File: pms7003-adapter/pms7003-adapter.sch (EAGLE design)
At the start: 8 parts, among them J1 LPPB052CFFN-RC, U1 WEMOS-D1-MINI, U2 ATECC508A-SSHDA-T

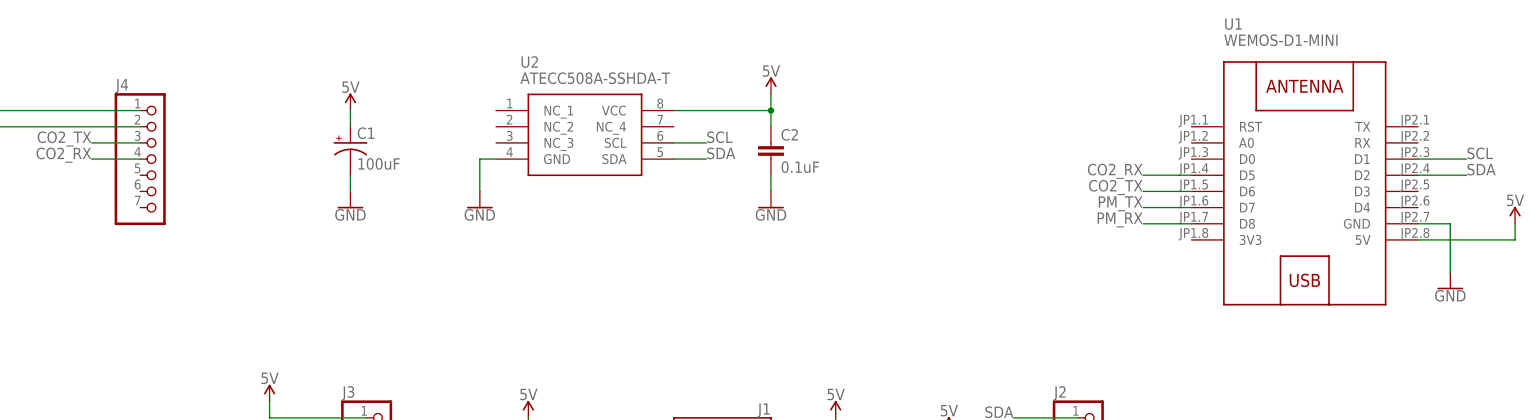
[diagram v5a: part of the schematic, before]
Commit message: Resized CO2 sensor connector, ripped up all traces for redesign
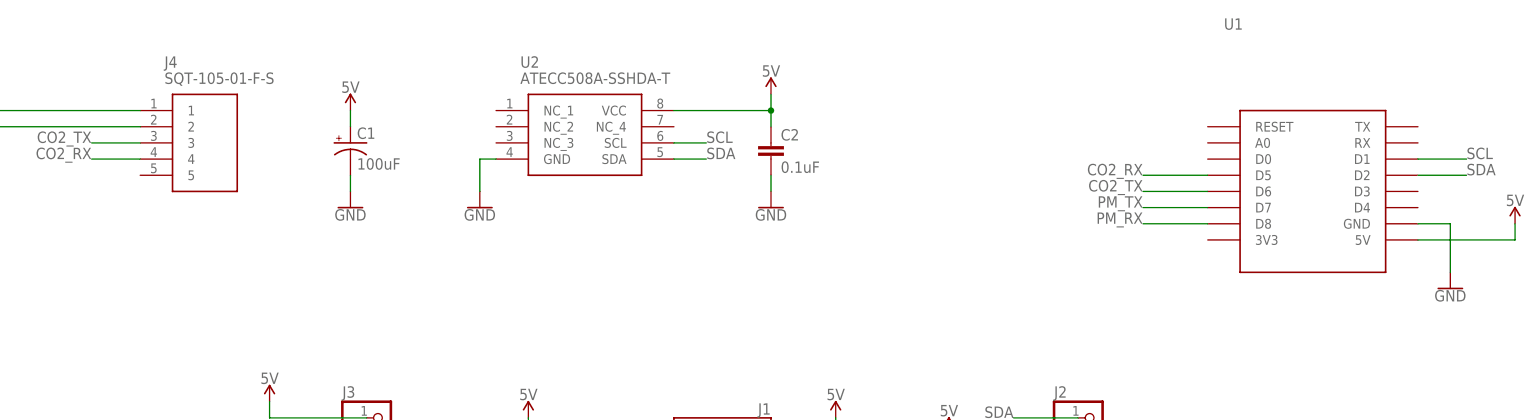
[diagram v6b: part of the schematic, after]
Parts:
- J4: value (none) -> SQT-105-01-F-S; device pinhead:PINHD-1X7 -> aqm-parts:SQT-105-01-F-S
- U1: value WEMOS-D1-MINI -> (none)
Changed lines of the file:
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@@
 <?xml version="1.0" encoding="utf-8"?>
 <!DOCTYPE eagle SYSTEM "eagle.dtd">
-<eagle version="9.6.1">
+<eagle version="9.6.2">
 <drawing>
 <settings>
@@
 <part name="SUPPLY2" library="SparkFun-PowerSymbols" library_urn="urn:adsk.eagle:library:530" deviceset="5V" device=""/>
 <part name="GND1" library="SparkFun-PowerSymbols" deviceset="GND" device=""/>
-<part name="J4" library="pinhead" library_urn="urn:adsk.eagle:library:325" deviceset="PINHD-1X7" device="" package3d_urn="urn:adsk.eagle:package:22477/2"/>
 <part name="SUPPLY1" library="SparkFun-PowerSymbols" library_urn="urn:adsk.eagle:library:530" deviceset="5V" device=""/>
 <part name="GND4" library="SparkFun-PowerSymbols" deviceset="GND" device=""/>
+<part name="J4" library="aqm-parts" deviceset="SQT-105-01-F-S" device=""/>
 </parts>
 <sheets>
@@
 <attribute name="VALUE" x="40.64" y="9.906" size="1.778" layer="96" align="top-center"/>
 </instance>
-<instance part="U1" gate="G$1" x="114.3" y="55.88" smashed="yes">
+<instance part="U1" gate="D1" x="114.3" y="55.88" smashed="yes">
 <attribute name="NAME" x="101.6" y="81.28" size="1.778" layer="95"/>
 <attribute name="VALUE" x="101.6" y="78.74" size="1.778" layer="96"/>
@@
 <attribute name="VALUE" x="137.16" y="40.386" size="1.778" layer="96" align="top-center"/>
 </instance>
-<instance part="J4" gate="A" x="-66.04" y="60.96" smashed="yes">
-<attribute name="NAME" x="-72.39" y="71.755" size="1.778" layer="95"/>
-<attribute name="VALUE" x="-72.39" y="48.26" size="1.778" layer="96"/>
-</instance>
 <instance part="SUPPLY1" gate="G$1" x="-93.98" y="71.12" smashed="yes">
 <attribute name="VALUE" x="-93.98" y="73.914" size="1.778" layer="96" align="bottom-center"/>
@@
 <instance part="GND4" gate="1" x="-93.98" y="60.96" smashed="yes">
 <attribute name="VALUE" x="-93.98" y="60.706" size="1.778" layer="96" align="top-center"/>
+</instance>
+<instance part="J4" gate="G$1" x="-68.58" y="68.58" smashed="yes">
+<attribute name="NAME" x="-64.77" y="76.2" size="1.778" layer="95" align="center-left"/>
+<attribute name="VALUE" x="-64.77" y="73.66" size="1.778" layer="96" align="center-left"/>
 </instance>
 </instances>
@@
 </segment>
 <segment>
-<pinref part="U1" gate="G$1" pin="D8"/>
-<wire x1="96.52" y1="50.8" x2="88.9" y2="50.8" width="0.1524" layer="91"/>
+<pinref part="U1" gate="D1" pin="D8"/>
+<wire x1="99.06" y1="50.8" x2="88.9" y2="50.8" width="0.1524" layer="91"/>
 <label x="88.9" y="50.8" size="1.778" layer="95" rot="MR0"/>
 </segment>
@@
 </segment>
 <segment>
-<pinref part="U1" gate="G$1" pin="D7"/>
-<wire x1="96.52" y1="53.34" x2="88.9" y2="53.34" width="0.1524" layer="91"/>
+<pinref part="U1" gate="D1" pin="D7"/>
+<wire x1="99.06" y1="53.34" x2="88.9" y2="53.34" width="0.1524" layer="91"/>
 <label x="88.9" y="53.34" size="1.778" layer="95" rot="MR0"/>
 </segment>
@@
 </segment>
 <segment>
-<pinref part="U1" gate="G$1" pin="GND"/>
+<pinref part="U1" gate="D1" pin="GND"/>
 <wire x1="132.08" y1="50.8" x2="137.16" y2="50.8" width="0.1524" layer="91"/>
 <pinref part="GND1" gate="1" pin="GND"/>
@@
 <pinref part="GND4" gate="1" pin="GND"/>
 <wire x1="-93.98" y1="63.5" x2="-93.98" y2="66.04" width="0.1524" layer="91"/>
-<pinref part="J4" gate="A" pin="2"/>
 <wire x1="-93.98" y1="66.04" x2="-68.58" y2="66.04" width="0.1524" layer="91"/>
+<pinref part="J4" gate="G$1" pin="2"/>
 </segment>
 </net>
@@
 </segment>
 <segment>
-<pinref part="U1" gate="G$1" pin="5V"/>
+<pinref part="U1" gate="D1" pin="5V"/>
 <wire x1="132.08" y1="48.26" x2="147.32" y2="48.26" width="0.1524" layer="91"/>
 <pinref part="SUPPLY2" gate="G$1" pin="5V"/>
@@
 <pinref part="SUPPLY1" gate="G$1" pin="5V"/>
 <wire x1="-93.98" y1="71.12" x2="-93.98" y2="68.58" width="0.1524" layer="91"/>
-<pinref part="J4" gate="A" pin="1"/>
 <wire x1="-68.58" y1="68.58" x2="-93.98" y2="68.58" width="0.1524" layer="91"/>
+<pinref part="J4" gate="G$1" pin="1"/>
 </segment>
 </net>
@@
 </segment>
 <segment>
-<pinref part="U1" gate="G$1" pin="D2"/>
+<pinref part="U1" gate="D1" pin="D2"/>
 <wire x1="132.08" y1="58.42" x2="139.7" y2="58.42" width="0.1524" layer="91"/>
 <label x="139.7" y="58.42" size="1.778" layer="95"/>
@@
 </segment>
 <segment>
-<pinref part="U1" gate="G$1" pin="D1"/>
+<pinref part="U1" gate="D1" pin="D1"/>
 <wire x1="132.08" y1="60.96" x2="139.7" y2="60.96" width="0.1524" layer="91"/>
 <label x="139.7" y="60.96" size="1.778" layer="95"/>
@@
 <net name="CO2_TX" class="0">
 <segment>
-<pinref part="J4" gate="A" pin="3"/>
 <wire x1="-68.58" y1="63.5" x2="-76.2" y2="63.5" width="0.1524" layer="91"/>
 <label x="-76.2" y="63.5" size="1.778" layer="95" rot="MR0"/>
-</segment>
-<segment>
-<pinref part="U1" gate="G$1" pin="D6"/>
-<wire x1="96.52" y1="55.88" x2="88.9" y2="55.88" width="0.1524" layer="91"/>
+<pinref part="J4" gate="G$1" pin="3"/>
+</segment>
+<segment>
+<pinref part="U1" gate="D1" pin="D6"/>
+<wire x1="99.06" y1="55.88" x2="88.9" y2="55.88" width="0.1524" layer="91"/>
 <label x="88.9" y="55.88" size="1.778" layer="95" rot="MR0"/>
 </segment>
@@
 <net name="CO2_RX" class="0">
 <segment>
-<pinref part="J4" gate="A" pin="4"/>
 <wire x1="-68.58" y1="60.96" x2="-76.2" y2="60.96" width="0.1524" layer="91"/>
 <label x="-76.2" y="60.96" size="1.778" layer="95" rot="MR0"/>
-</segment>
-<segment>
-<pinref part="U1" gate="G$1" pin="D5"/>
-<wire x1="96.52" y1="58.42" x2="88.9" y2="58.42" width="0.1524" layer="91"/>
+<pinref part="J4" gate="G$1" pin="4"/>
+</segment>
+<segment>
+<pinref part="U1" gate="D1" pin="D5"/>
+<wire x1="99.06" y1="58.42" x2="88.9" y2="58.42" width="0.1524" layer="91"/>
 <label x="88.9" y="58.42" size="1.778" layer="95" rot="MR0"/>
 </segment>
@@
 </drawing>
 <compatibility>
+<note version="6.3" minversion="6.2.2" severity="warning">
+Since Version 6.2.2 text objects can contain more than one line,
+which will not be processed correctly with this version.
+</note>
 <note version="8.2" severity="warning">
 Since Version 8.2, EAGLE supports online libraries. The ids

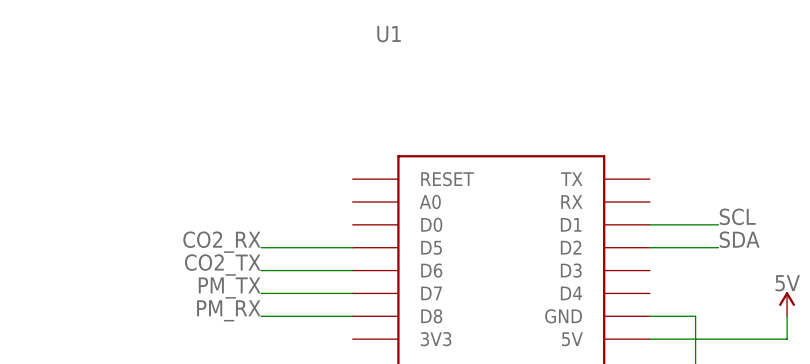
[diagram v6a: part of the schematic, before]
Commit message: Added an improved D1 mini footprint
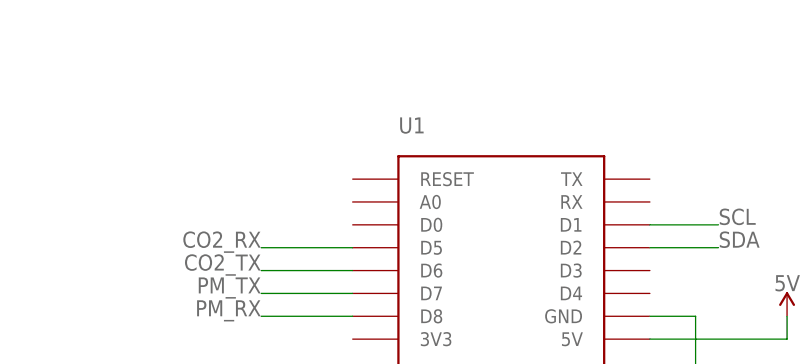
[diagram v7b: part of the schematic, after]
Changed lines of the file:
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@@
 </instance>
 <instance part="U1" gate="D1" x="114.3" y="55.88" smashed="yes">
-<attribute name="NAME" x="101.6" y="81.28" size="1.778" layer="95"/>
+<attribute name="NAME" x="104.14" y="71.12" size="1.778" layer="95"/>
 <attribute name="VALUE" x="101.6" y="78.74" size="1.778" layer="96"/>
 </instance>
@@
 </drawing>
 <compatibility>
-<note version="6.3" minversion="6.2.2" severity="warning">
-Since Version 6.2.2 text objects can contain more than one line,
-which will not be processed correctly with this version.
-</note>
 <note version="8.2" severity="warning">
 Since Version 8.2, EAGLE supports online libraries. The ids

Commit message: rev 2 board ready for fab!
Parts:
- added J5: (no value), pinhead:PINHD-1X5
- J4: value SQT-105-01-F-S -> SQT-107-01-F-S; device aqm-parts:SQT-105-01-F-S -> aqm-parts:SQT-107-01-F-S
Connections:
- net 5V: now also J5.1
- net CO2_RX: now also U1.D0; no longer U1.D5
- net CO2_TX: now also U1.D5; no longer U1.D6
- net GND: now also J5.2
- net PM_RX: now also U1.D7; no longer U1.D8
- net PM_TX: now also U1.D6; no longer U1.D7
- net SCL: now also J5.3
- net SDA: now also J5.4
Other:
- moved on the sheet: U1
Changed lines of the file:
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@@
 <part name="SUPPLY1" library="SparkFun-PowerSymbols" library_urn="urn:adsk.eagle:library:530" deviceset="5V" device=""/>
 <part name="GND4" library="SparkFun-PowerSymbols" deviceset="GND" device=""/>
-<part name="J4" library="aqm-parts" deviceset="SQT-105-01-F-S" device=""/>
+<part name="J4" library="aqm-parts" deviceset="SQT-107-01-F-S" device=""/>
+<part name="J5" library="pinhead" library_urn="urn:adsk.eagle:library:325" deviceset="PINHD-1X5" device="" package3d_urn="urn:adsk.eagle:package:22469/2"/>
+<part name="SUPPLY5" library="SparkFun-PowerSymbols" library_urn="urn:adsk.eagle:library:530" deviceset="5V" device=""/>
+<part name="GND6" library="SparkFun-PowerSymbols" deviceset="GND" device=""/>
 </parts>
 <sheets>
@@
 <attribute name="VALUE" x="40.64" y="9.906" size="1.778" layer="96" align="top-center"/>
 </instance>
-<instance part="U1" gate="D1" x="114.3" y="55.88" smashed="yes">
-<attribute name="NAME" x="104.14" y="71.12" size="1.778" layer="95"/>
-<attribute name="VALUE" x="101.6" y="78.74" size="1.778" layer="96"/>
-</instance>
-<instance part="SUPPLY2" gate="G$1" x="147.32" y="50.8" smashed="yes">
-<attribute name="VALUE" x="147.32" y="53.594" size="1.778" layer="96" align="bottom-center"/>
-</instance>
-<instance part="GND1" gate="1" x="137.16" y="40.64" smashed="yes">
-<attribute name="VALUE" x="137.16" y="40.386" size="1.778" layer="96" align="top-center"/>
+<instance part="U1" gate="D1" x="88.9" y="60.96" smashed="yes">
+<attribute name="NAME" x="78.74" y="76.2" size="1.778" layer="95"/>
+<attribute name="VALUE" x="76.2" y="83.82" size="1.778" layer="96"/>
+</instance>
+<instance part="SUPPLY2" gate="G$1" x="121.92" y="55.88" smashed="yes">
+<attribute name="VALUE" x="121.92" y="58.674" size="1.778" layer="96" align="bottom-center"/>
+</instance>
+<instance part="GND1" gate="1" x="111.76" y="45.72" smashed="yes">
+<attribute name="VALUE" x="111.76" y="45.466" size="1.778" layer="96" align="top-center"/>
 </instance>
 <instance part="SUPPLY1" gate="G$1" x="-93.98" y="71.12" smashed="yes">
@@
 </instance>
 <instance part="J4" gate="G$1" x="-68.58" y="68.58" smashed="yes">
-<attribute name="NAME" x="-64.77" y="76.2" size="1.778" layer="95" align="center-left"/>
-<attribute name="VALUE" x="-64.77" y="73.66" size="1.778" layer="96" align="center-left"/>
+<attribute name="NAME" x="-67.31" y="76.2" size="1.778" layer="95" align="center-left"/>
+<attribute name="VALUE" x="-67.31" y="73.66" size="1.778" layer="96" align="center-left"/>
+</instance>
+<instance part="J5" gate="A" x="-73.66" y="15.24" smashed="yes">
+<attribute name="NAME" x="-80.01" y="23.495" size="1.778" layer="95"/>
+<attribute name="VALUE" x="-80.01" y="5.08" size="1.778" layer="96"/>
+</instance>
+<instance part="SUPPLY5" gate="G$1" x="-91.44" y="22.86" smashed="yes">
+<attribute name="VALUE" x="-91.44" y="25.654" size="1.778" layer="96" align="bottom-center"/>
+</instance>
+<instance part="GND6" gate="1" x="-91.44" y="5.08" smashed="yes">
+<attribute name="VALUE" x="-91.44" y="4.826" size="1.778" layer="96" align="top-center"/>
 </instance>
 </instances>
@@
 </segment>
 <segment>
-<pinref part="U1" gate="D1" pin="D8"/>
-<wire x1="99.06" y1="50.8" x2="88.9" y2="50.8" width="0.1524" layer="91"/>
-<label x="88.9" y="50.8" size="1.778" layer="95" rot="MR0"/>
+<pinref part="U1" gate="D1" pin="D7"/>
+<wire x1="73.66" y1="58.42" x2="68.58" y2="58.42" width="0.1524" layer="91"/>
+<label x="68.58" y="58.42" size="1.778" layer="95" rot="MR0"/>
 </segment>
 </net>
@@
 </segment>
 <segment>
-<pinref part="U1" gate="D1" pin="D7"/>
-<wire x1="99.06" y1="53.34" x2="88.9" y2="53.34" width="0.1524" layer="91"/>
-<label x="88.9" y="53.34" size="1.778" layer="95" rot="MR0"/>
+<pinref part="U1" gate="D1" pin="D6"/>
+<wire x1="73.66" y1="60.96" x2="68.58" y2="60.96" width="0.1524" layer="91"/>
+<label x="68.58" y="60.96" size="1.778" layer="95" rot="MR0"/>
 </segment>
 </net>
@@
 <segment>
 <pinref part="U1" gate="D1" pin="GND"/>
-<wire x1="132.08" y1="50.8" x2="137.16" y2="50.8" width="0.1524" layer="91"/>
+<wire x1="106.68" y1="55.88" x2="111.76" y2="55.88" width="0.1524" layer="91"/>
 <pinref part="GND1" gate="1" pin="GND"/>
-<wire x1="137.16" y1="50.8" x2="137.16" y2="43.18" width="0.1524" layer="91"/>
+<wire x1="111.76" y1="55.88" x2="111.76" y2="48.26" width="0.1524" layer="91"/>
 </segment>
 <segment>
@@
 <wire x1="-93.98" y1="66.04" x2="-68.58" y2="66.04" width="0.1524" layer="91"/>
 <pinref part="J4" gate="G$1" pin="2"/>
+</segment>
+<segment>
+<pinref part="J5" gate="A" pin="2"/>
+<wire x1="-76.2" y1="17.78" x2="-91.44" y2="17.78" width="0.1524" layer="91"/>
+<pinref part="GND6" gate="1" pin="GND"/>
+<wire x1="-91.44" y1="17.78" x2="-91.44" y2="7.62" width="0.1524" layer="91"/>
 </segment>
 </net>
@@
 <segment>
 <pinref part="U1" gate="D1" pin="5V"/>
-<wire x1="132.08" y1="48.26" x2="147.32" y2="48.26" width="0.1524" layer="91"/>
+<wire x1="106.68" y1="53.34" x2="121.92" y2="53.34" width="0.1524" layer="91"/>
 <pinref part="SUPPLY2" gate="G$1" pin="5V"/>
-<wire x1="147.32" y1="48.26" x2="147.32" y2="50.8" width="0.1524" layer="91"/>
+<wire x1="121.92" y1="53.34" x2="121.92" y2="55.88" width="0.1524" layer="91"/>
 </segment>
 <segment>
@@
 <pinref part="J4" gate="G$1" pin="1"/>
 </segment>
+<segment>
+<pinref part="J5" gate="A" pin="1"/>
+<wire x1="-76.2" y1="20.32" x2="-91.44" y2="20.32" width="0.1524" layer="91"/>
+<pinref part="SUPPLY5" gate="G$1" pin="5V"/>
+<wire x1="-91.44" y1="20.32" x2="-91.44" y2="22.86" width="0.1524" layer="91"/>
+</segment>
 </net>
 <net name="SDA" class="0">
@@
 <segment>
 <pinref part="U1" gate="D1" pin="D2"/>
-<wire x1="132.08" y1="58.42" x2="139.7" y2="58.42" width="0.1524" layer="91"/>
-<label x="139.7" y="58.42" size="1.778" layer="95"/>
+<wire x1="106.68" y1="63.5" x2="114.3" y2="63.5" width="0.1524" layer="91"/>
+<label x="114.3" y="63.5" size="1.778" layer="95"/>
+</segment>
+<segment>
+<pinref part="J5" gate="A" pin="4"/>
+<wire x1="-76.2" y1="12.7" x2="-83.82" y2="12.7" width="0.1524" layer="91"/>
+<label x="-83.82" y="12.7" size="1.778" layer="95" rot="MR0"/>
 </segment>
 </net>
@@
 <segment>
 <pinref part="U1" gate="D1" pin="D1"/>
-<wire x1="132.08" y1="60.96" x2="139.7" y2="60.96" width="0.1524" layer="91"/>
-<label x="139.7" y="60.96" size="1.778" layer="95"/>
+<wire x1="106.68" y1="66.04" x2="114.3" y2="66.04" width="0.1524" layer="91"/>
+<label x="114.3" y="66.04" size="1.778" layer="95"/>
+</segment>
+<segment>
+<pinref part="J5" gate="A" pin="3"/>
+<wire x1="-76.2" y1="15.24" x2="-83.82" y2="15.24" width="0.1524" layer="91"/>
+<label x="-83.82" y="15.24" size="1.778" layer="95" rot="MR0"/>
 </segment>
 </net>
@@
 </segment>
 <segment>
-<pinref part="U1" gate="D1" pin="D6"/>
-<wire x1="99.06" y1="55.88" x2="88.9" y2="55.88" width="0.1524" layer="91"/>
-<label x="88.9" y="55.88" size="1.778" layer="95" rot="MR0"/>
+<pinref part="U1" gate="D1" pin="D5"/>
+<wire x1="73.66" y1="63.5" x2="68.58" y2="63.5" width="0.1524" layer="91"/>
+<label x="68.58" y="63.5" size="1.778" layer="95" rot="MR0"/>
 </segment>
 </net>
@@
 </segment>
 <segment>
-<pinref part="U1" gate="D1" pin="D5"/>
-<wire x1="99.06" y1="58.42" x2="88.9" y2="58.42" width="0.1524" layer="91"/>
-<label x="88.9" y="58.42" size="1.778" layer="95" rot="MR0"/>
-</segment>
-</net>
+<pinref part="U1" gate="D1" pin="D0"/>
+<wire x1="73.66" y1="66.04" x2="68.58" y2="66.04" width="0.1524" layer="91"/>
+<label x="68.58" y="66.04" size="1.778" layer="95" rot="MR0"/>
+</segment>
+</net>
